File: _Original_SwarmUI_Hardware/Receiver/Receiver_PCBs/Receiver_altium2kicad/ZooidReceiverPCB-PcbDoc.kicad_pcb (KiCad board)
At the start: 4 copper layers, 59.4 x 13.3 mm, 45 parts, among them J1 Molex 48037-2200 USB Type A R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, P1 TagConnector TC2030-IDC-NL, U1 QFN, 48-Leads, Body 7,00x7,00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, U2 . 6-Lead Lead Frame Chip Scal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, U3 QFN, 20-Leads, Body 4,00x4,00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

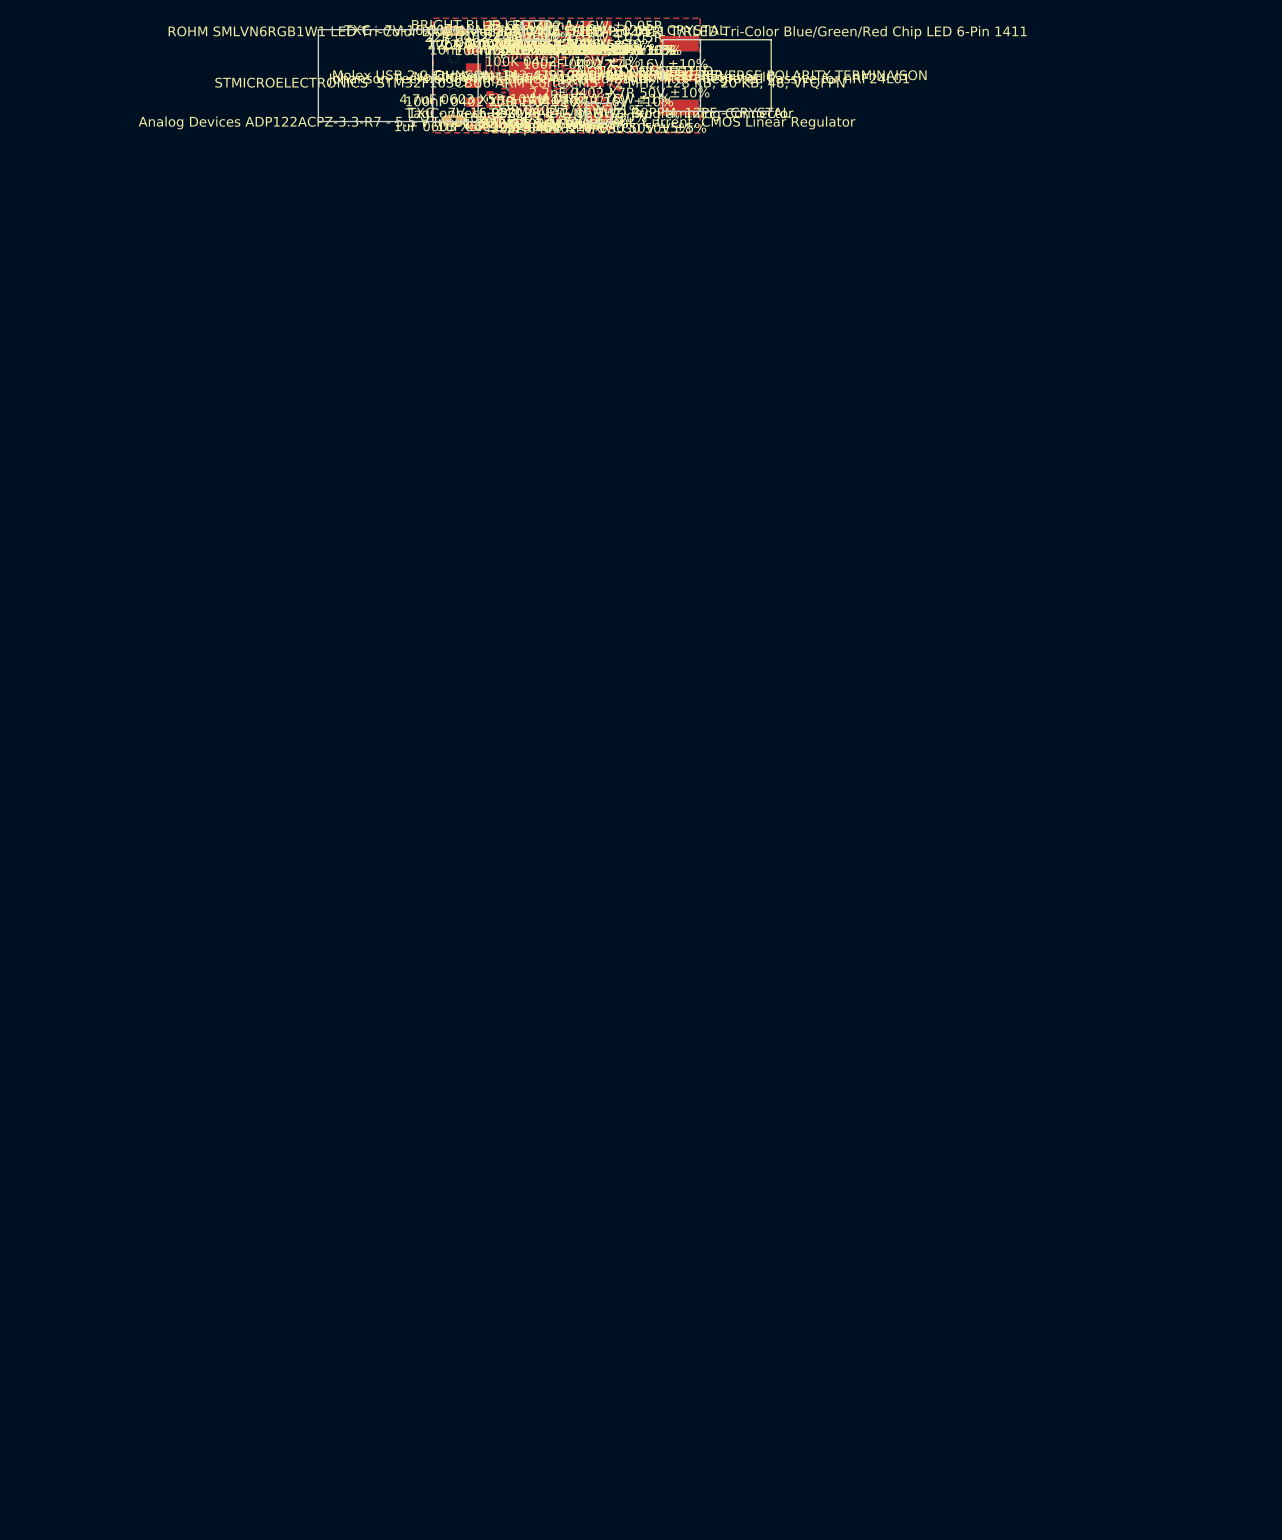
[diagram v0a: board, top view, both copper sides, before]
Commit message: Changed PCB for more compact component placement, shortened board 3, added images for the new layout
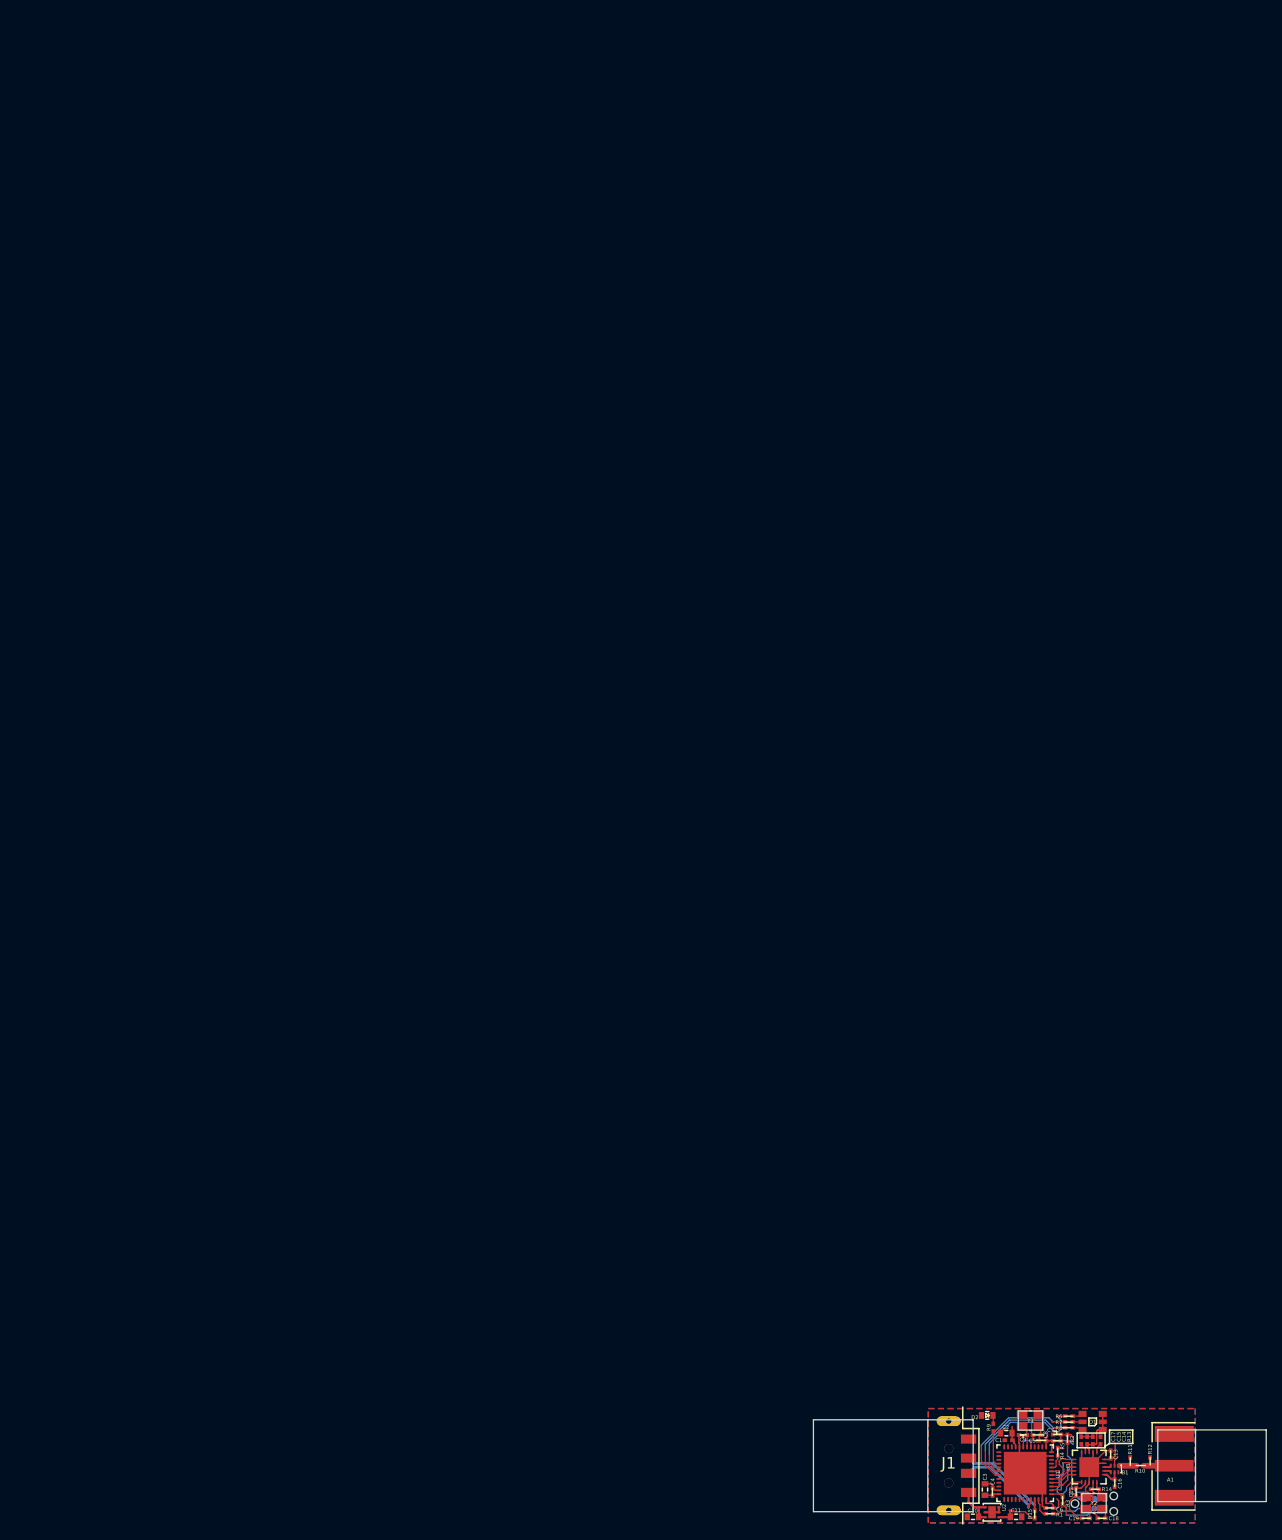
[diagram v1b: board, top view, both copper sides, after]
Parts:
- A1: value (none) -> JOHNSON 142-4701-801 SMA FEMELLE REVERSE POLARITY TERMINAISON
- B1: value 2.45 GHz Impedance Matched Balun-Filter: Optimized for Nordic's Chipset nRF24L01 -> Johanson Technology Impedance Matched Balun Filter Integrated Passive for nRF24L01
- C1, C12, C13, C14, C15, C16, C17, C18, C19, C4, C5, C6, C7, C8, C9, R1, R10, R13, R14, R15, R2, R3, R4, R5, R6, R7, R8, R9: value Chip Body 1.0 x 0.5 mm (LxW typ) -> (none)
- C10, C11, C2, C3: value Chip Body 1.6 x 0.8 mm (LxW typ) -> (none)
- D1: value 3.5 x 2.8 mm 6-SMD Flat Leads -> ROHM SMLVN6RGB1W1 LED Tri-Color Blue/Green/Red Chip LED 6-Pin 1411 T/RLED Tri-Color Blue/Green/Red Chip LED 6-Pin 1411
- D2: value Chip Body 1.6 x 0.8 mm (LxW typ) -> BRIGHT BLUE LED 20mA
- J1: value Molex 48037-2200 USB Type A Receptacle -> Molex USB 2.0 Connector Plug USB Type A
- P1: value TagConnector TC2030-IDC-NL -> TagConnect TC2030-IDC-NL SWD Programming Connector
- R11, R12: value Chip Body 1.0 x 0.5 mm (LxW typ) -> NOT CONNECTED
- U1: value QFN, 48-Leads, Body 7,00x7,00mm, Pitch 0,50mm, Thermal Pad 5,60x5,60mm, IPC High Density -> STMICROELECTRONICS STM32F103CBU6 ARM Cortex-M3, 72 MHz, 128 KB, 20 KB, 48, VFQFPN
- U2: value . 6-Lead Lead Frame Chip Scale Package [LFCSP_UD] 2.00 mm× 2.00 mm Body, Ultra Thin, Dual Lead (CP-6-3) -> Analog Devices ADP122ACPZ-3.3-R7 - 5.5 V Input, 300 mA, Low Quiescent Current, CMOS Linear Regulator
- U3: value QFN, 20-Leads, Body 4,00x4,00mm, Pitch 0,50mm, Thermal Pad 2,60x2,60mm, IPC High Density -> Nordic Semi Ultra low power 2.4GHz RF Transceiver IC
- Y1, Y2: value (none) -> TXC - 7V-16.000MAAE-T, 16MHZ, 30PPM, 12PF - CRYSTAL
- moved R5 193.5 mm to (146.8, 96.6)
- moved A1 193.5 mm to (162.2, 99.8)
- moved B1 193.5 mm to (154.4, 100.3)
- moved C1 193.5 mm to (140.5, 96.5)
- moved C10 193.5 mm to (135.8, 106.5)
- moved C11 193.5 mm to (141.4, 106.5)
- moved C12 193.5 mm to (149.3, 103.3)
- moved C13 193.5 mm to (153.8, 98.4)
- moved C14 193.5 mm to (151.5, 96.5)
- moved C15 193.5 mm to (150.7, 96.5)
- moved C16 193.5 mm to (154.4, 102.1)
- moved C17 193.5 mm to (150.0, 96.5)
- moved C18 193.5 mm to (152.7, 106.7)
- moved C19 193.5 mm to (150.6, 106.7)
- moved C2 193.5 mm to (140.2, 95.6)
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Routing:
- net Net1: track 771.2 -> 575.7 mm
- net GND: track 0.00 -> 42.6 mm
- net +3.3V: track 0.00 -> 34.7 mm
- net NetP1_3: track 0.00 -> 9.69 mm
- net RGBLED1: track 0.00 -> 6.65 mm
- net RADIO_X1_16MHZ: track 0.00 -> 5.72 mm
- net VUSB: track 0.00 -> 5.71 mm
- net RADIO_X2_16MHZ: track 0.00 -> 5.69 mm
- net NetP1_4: track 0.00 -> 5.67 mm
- net RADIO_SPI.CE: track 0.00 -> 5.64 mm
- net RGBLED3: track 0.00 -> 5.37 mm
- net MCU_X1_16MHZ: track 0.00 -> 4.84 mm
- net STATUS_LED: track 0.00 -> 4.74 mm
- net NetP1_2: track 0.00 -> 4.39 mm
- net NRST: track 0.00 -> 4.39 mm
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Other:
- outline, holes or cut-outs redrawn
